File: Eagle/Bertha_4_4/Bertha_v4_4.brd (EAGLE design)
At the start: 100 x 84.6 mm, 115 parts, among them CON1 JACK_DC_BARREL, IC1 MCP1703DB, J1 RJ12RIGHTANGLE-I2C, J2 RJ12RIGHTANGLE-I2C, J7 22--02, Q1 BSP75, Q2 BSP75, Q3 BSP75, Q4 BSP75, Q5 BSP75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

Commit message: Added protection diode on 12V line closes #26
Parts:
- added D1: 1N581D1206, lpatiny:LED-1206
- moved C2 7.70 mm to (29.0, 15.3), flipped to the top, turned to 180 degrees
- moved CU4 7.66 mm to (29.1, 12.6), flipped to the top, turned to 180 degrees
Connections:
- new net VDD: C1.1, CU3.1, CU7.1, D1.C, D2.C, D4.C, IC1.1, R12.2, X3.1, X3.2
- net +12V: now also D1.A; no longer C1.1, CU3.1, CU7.1, D2.C, D4.C, IC1.1, R12.2, X3.1, X3.2
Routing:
- net VDD: track 0.00 -> 168.8 mm, vias 0 -> 2
- net +12V: track 334.4 -> 177.1 mm, vias 2 -> 0
- net GND: track 175.2 -> 177.3 mm, vias 39 -> 41
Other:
- board text added: "12V or USB"
- board text removed: "12V"

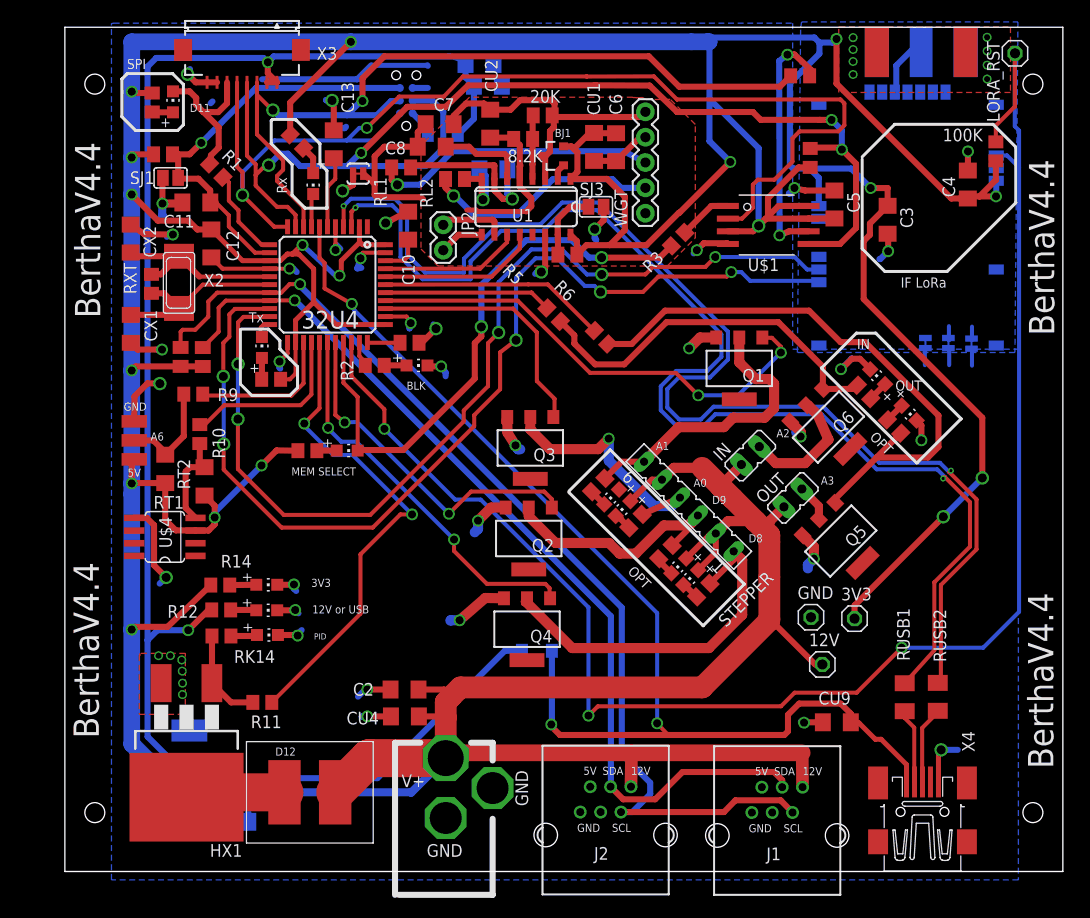
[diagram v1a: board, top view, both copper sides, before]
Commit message: 4mm holes on mainboard
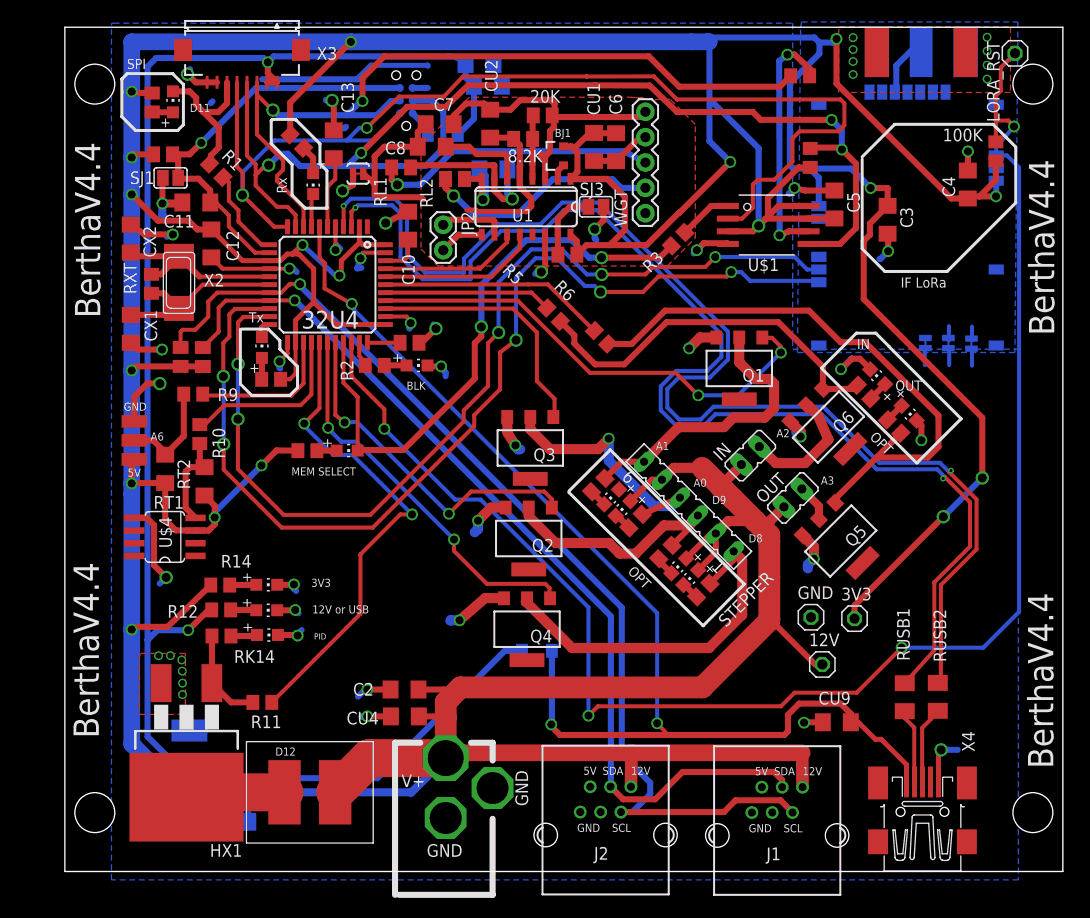
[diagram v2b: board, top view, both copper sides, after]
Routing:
- net D5*: track 164.8 -> 158.9 mm, vias 3 -> 4
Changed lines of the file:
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@@
 <text x="67.62685" y="41.421275" size="0.8128" layer="25" rot="R180">A2</text>
 <text x="9.567934375" y="74.024946875" size="0.8128" layer="25" rot="R180">D11</text>
-<hole x="-2" y="76" drill="2"/>
-<hole x="92" y="76" drill="2"/>
-<hole x="-2" y="3" drill="2"/>
-<hole x="92" y="3" drill="2"/>
+<hole x="-2" y="76" drill="4"/>
+<hole x="92" y="76" drill="4"/>
+<hole x="-2" y="3" drill="4"/>
+<hole x="92" y="3" drill="4"/>
 <text x="94.049428125" y="7.40274375" size="2.54" layer="25" rot="R90">BerthaV4.4</text>
 <text x="-1.595646875" y="10.453128125" size="2.54" layer="25" rot="R90">BerthaV4.4</text>
@@
 <wire x1="78.848225" y1="19.527221875" x2="87.0215875" y2="19.527221875" width="0.4064" layer="16"/>
 <wire x1="87.0215875" y1="19.527221875" x2="90.616096875" y2="23.12173125" width="0.4064" layer="16"/>
-<wire x1="90.207996875" y1="79.087009375" x2="90.185946875" y2="77.428159375" width="0.4064" layer="16"/>
-<wire x1="90.185946875" y1="77.428159375" x2="90.185946875" y2="71.779446875" width="0.4064" layer="16"/>
-<wire x1="90.185946875" y1="71.779446875" x2="90.616096875" y2="71.349296875" width="0.4064" layer="16"/>
-<wire x1="90.616096875" y1="71.349296875" x2="90.616096875" y2="67.639684375" width="0.4064" layer="16"/>
 <wire x1="90.616096875" y1="67.639684375" x2="90.616096875" y2="23.12173125" width="0.4064" layer="16"/>
 <wire x1="88.327190625" y1="68.851403125" x2="89.404378125" y2="68.851403125" width="0.4064" layer="16"/>
 <wire x1="89.404378125" y1="68.851403125" x2="90.616096875" y2="67.639684375" width="0.4064" layer="16"/>
-<wire x1="88.286534375" y1="70.2136375" x2="88.286534375" y2="71.847665625" width="0.4064" layer="1"/>
-<wire x1="88.286534375" y1="71.847665625" x2="90.185946875" y2="73.747078125" width="0.4064" layer="1"/>
-<wire x1="90.185946875" y1="73.747078125" x2="90.185946875" y2="79.064959375" width="0.4064" layer="1"/>
 <wire x1="90.185946875" y1="79.064959375" x2="90.207996875" y2="79.087009375" width="0.4064" layer="1"/>
+<wire x1="88.286534375" y1="70.2136375" x2="88.286534375" y2="72.348403125" width="0.4064" layer="1"/>
+<wire x1="88.286534375" y1="72.348403125" x2="88.286534375" y2="74.830703125" width="0.4064" layer="1"/>
+<wire x1="88.286534375" y1="74.830703125" x2="88.782459375" y2="75.326628125" width="0.4064" layer="1"/>
+<wire x1="88.782459375" y1="75.326628125" x2="88.782459375" y2="77.661471875" width="0.4064" layer="1"/>
+<wire x1="88.782459375" y1="77.661471875" x2="90.207996875" y2="79.087009375" width="0.4064" layer="1"/>
+<wire x1="90.207996875" y1="79.087009375" x2="90.207996875" y2="79.0566125" width="0.4064" layer="16"/>
+<wire x1="88.327190625" y1="68.851403125" x2="88.327190625" y2="69.6968375" width="0.4064" layer="16"/>
+<wire x1="88.327190625" y1="69.6968375" x2="90.10440625" y2="71.75225625" width="0.4064" layer="16"/>
+<via x="90.10440625" y="71.75225625" extent="1-16" drill="0.8"/>
+<wire x1="90.10440625" y1="71.75225625" x2="89.54505625" y2="72.348403125" width="0.4064" layer="1"/>
+<wire x1="89.54505625" y1="72.348403125" x2="88.286534375" y2="72.348403125" width="0.4064" layer="1"/>
 </signal>
 <signal name="VUSB">

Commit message: Added jack connector for PID closes #40
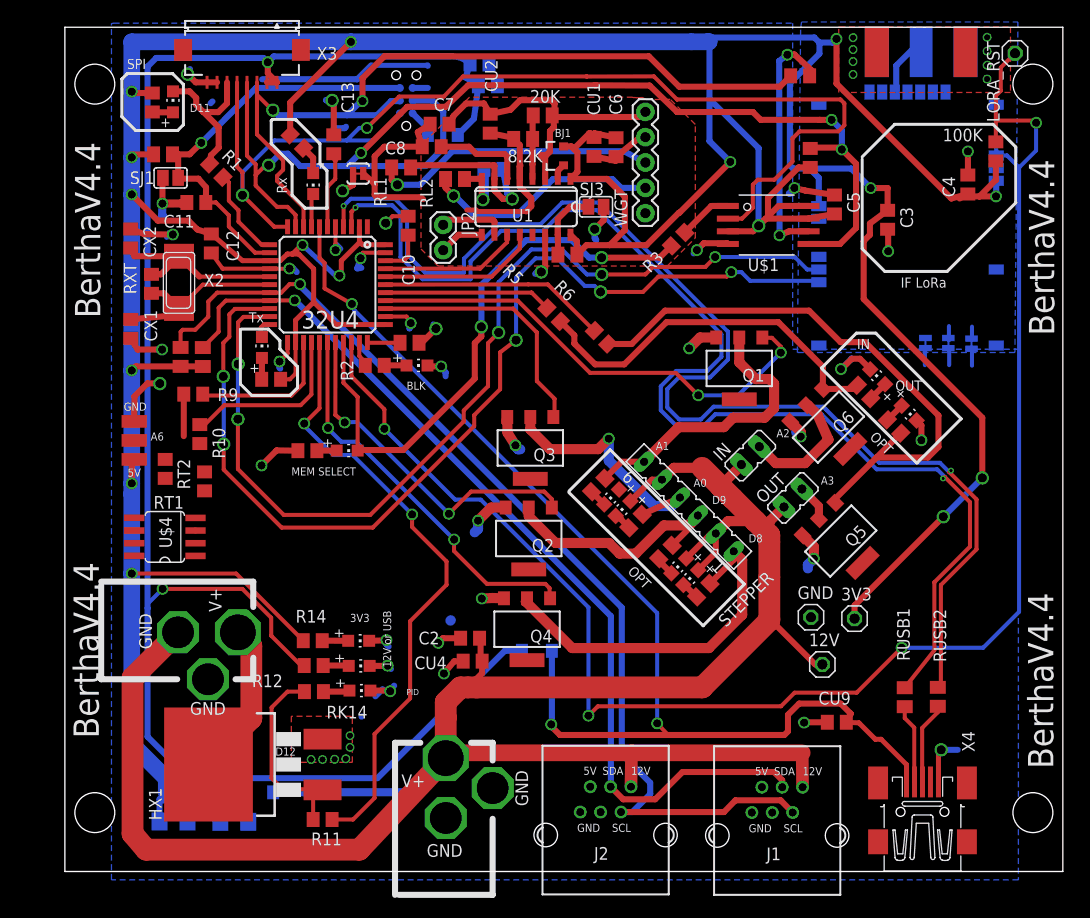
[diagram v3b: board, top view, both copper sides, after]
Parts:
- removed J7: 22--02, lpatiny:2-PIN-5.08S
- added CON2: JACK_DC_BARREL, lpatiny:DC_BARREL
- C1, C10, C11, C12, C13, C2, C3, C4, C5, C6, C7, C8, C9, CU1, CU2, CU3, CU4, CU9, CX1, CX2: device rcl:C1206 -> rcl:C0805
- RT1, RT2: device resistor:R1206 -> resistor:R0805
- RUSB1, RUSB2: device resistor:M1206 -> resistor:M0805
- moved R11 13.2 mm to (20.8, 2.31)
- moved LDPID 10.8 mm to (24.6, 15.2)
- moved LDPW12 10.8 mm to (24.5, 17.7)
- moved R12 10.8 mm to (19.9, 17.7)
- moved R14 10.8 mm to (19.8, 20.2)
- moved RK14 10.8 mm to (20.0, 15.1)
- moved LDPW3 10.8 mm to (24.4, 20.2)
- moved CU4 8.76 mm to (35.9, 18.2)
- moved C2 8.34 mm to (35.6, 20.5)
- moved HX1 4.80 mm to (11.9, 7.82), turned to 90 degrees
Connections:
- removed net N$36: HX1.2, J7.2
- new net N$2: CON2.P$1, HX1.2
- net +12V: now also CON2.P$2; no longer J7.1
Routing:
- net +12V: track 177.1 -> 223.0 mm
- net N$2: track 0.00 -> 15.6 mm
- net VDD: track 168.8 -> 184.0 mm
- net D6*: track 48.8 -> 61.4 mm
- net 3.3V: track 483.8 -> 471.7 mm, vias 18 -> 17
- net GND: track 177.3 -> 165.9 mm, vias 41 -> 40
- net N$6: track 10.5 -> 21.9 mm
- net N$36: track 10.0 -> 0.00 mm
- net N$9: track 9.69 -> 0.00 mm
- net N$21: track 10.8 -> 4.20 mm
- net D5*: track 158.9 -> 163.4 mm
- net LGND: track 35.7 -> 36.7 mm
- net VUSB: track 116.3 -> 116.9 mm
- net N$5: track 30.6 -> 31.1 mm

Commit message: Changed pin Mapping to allow PWM food control Need to Adapat Arduino code !!!
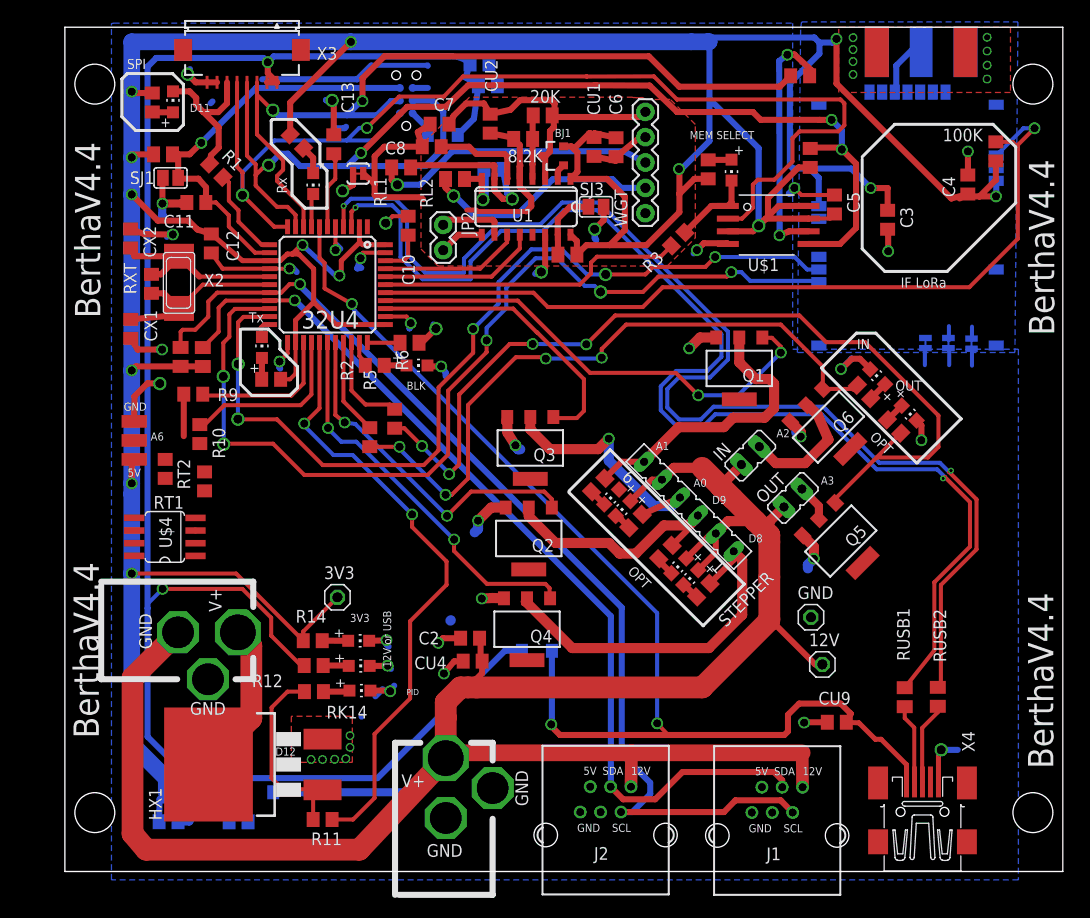
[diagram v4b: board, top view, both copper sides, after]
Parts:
- removed LORA_RST: (no value), Headerlibrary:1X01
- CU7, CU8: device rcl:C1206 -> rcl:C0805
- moved 3V3 51.9 mm to (22.3, 24.6)
- moved RK19 49.1 mm to (59.5, 67.5), turned to 90 degrees
- moved LDMEM 47.7 mm to (61.8, 67.4), turned to 180 degrees
- moved R6 22.2 mm to (28.0, 42.5), turned to 270 degrees
- moved R5 22.1 mm to (25.6, 40.6), turned to 270 degrees
- moved CU8 0.50 mm to (5.39, 2.09)
- moved CU7 0.44 mm to (12.4, 2.08)
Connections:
- removed net N$10: R3.1, U$1.CE
- new net MEM_SEL: LDMEM.C, R3.1, U$1.CE
- net A2: now also 100K.2, U100.P$32; no longer R5.1
- net A3: now also R3.2; no longer R6.1
- net D10*: now also R5.1; no longer LDMEM.C, R3.2
- net D5*: now also R6.1; no longer 100K.2, LORA_RST.1, U100.P$32
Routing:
- net D5*: track 163.4 -> 9.92 mm, vias 4 -> 0
- net A2: track 16.8 -> 86.0 mm, vias 0 -> 1
- net 3.3V: track 471.7 -> 423.1 mm, vias 17 -> 14
- net D10*: track 57.9 -> 9.63 mm, vias 2 -> 0
- net N$11: track 58.4 -> 91.1 mm, vias 0 -> 4
- net N$8: track 38.0 -> 67.1 mm, vias 0 -> 4
- net MEM_SEL: track 0.00 -> 8.10 mm
- net A3: track 22.9 -> 30.9 mm
- net TX: track 97.7 -> 90.8 mm
- net RX: track 102.3 -> 96.5 mm
- net N$10: track 5.41 -> 0.00 mm
- net A0: track 26.2 -> 29.9 mm
- net GND: track 165.9 -> 167.1 mm

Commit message: Added Jack connector for DS18B20 closes #24
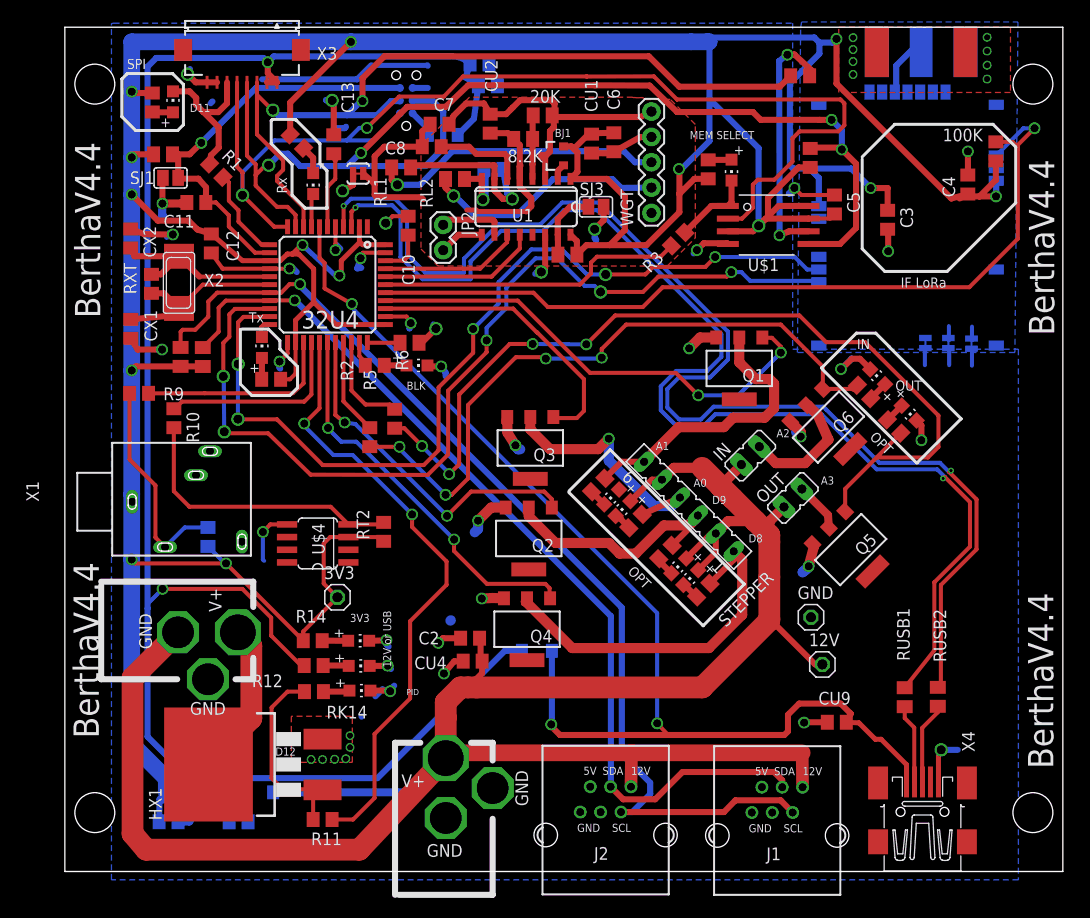
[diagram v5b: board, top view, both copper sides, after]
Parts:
- removed U$8: DS18B20_SMALLPADS, lpatiny:SMALLPADS_X3
- added X1: 1503_09, con-lumberg:1503_09
- moved RT2 18.6 mm to (26.9, 31.1)
- moved U$4 15.3 mm to (20.3, 31.9)
- moved RT1 8.05 mm to (9.34, 30.6), flipped to the bottom
- moved R9 5.43 mm to (2.43, 45.0)
- moved R10 3.05 mm to (5.92, 42.5)
- moved Q5 1.31 mm to (73.7, 29.4)
- moved WGT 0.61 mm to (53.8, 63.1)
- moved C6 0.54 mm to (50.0, 70.2)
- moved CU1 0.41 mm to (47.8, 70.0)
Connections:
- net 3.3V: now also X1.1; no longer U$8.PIN3
- net GND: now also X1.3; no longer U$8.PIN1
- net N$21: now also X1.2; no longer U$8.PIN2
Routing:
- net N$9: track 0.00 -> 28.8 mm
- net N$21: track 4.20 -> 22.0 mm
- net 3.3V: track 423.1 -> 435.2 mm
- net A6: track 14.8 -> 20.0 mm
- net D12*: track 17.7 -> 19.6 mm
- net N$13: track 3.73 -> 4.97 mm
- net RX: track 96.5 -> 95.7 mm
- net A-: track 28.6 -> 29.3 mm
- net N$5: track 31.1 -> 31.7 mm
- net A+: track 23.9 -> 24.5 mm
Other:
- board text removed: "5V"
- board text removed: "A6"
- board text removed: "GND"
